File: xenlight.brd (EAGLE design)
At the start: 160.2 x 80.2 mm, 33 parts, among them IC1 MEGA16-A, IC14 FT232RL, IC2 74HC573D, IC3 74HC573D, IC4 74HC573D, IC5 74HC573D, IC6 74HC573D, IC7 74HC573D, X1 057-010-1, X2 057-010-1, X3 057-010-1, X4 057-010-1, X5 057-010-1, X6 057-010-1, X7 KUSBVX

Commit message: Second version of board, not for homemade production.
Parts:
- moved IC11 60.2 mm to (117.9, 68.4)
- moved X9 39.1 mm to (75.3, 8.61)
- moved IC4 38.6 mm to (100.8, 69.1), turned to 270 degrees
- moved R7 37.7 mm to (43.7, 15.5), turned to 0 degrees
- moved C5 34.8 mm to (46.8, 18.5), turned to 180 degrees
- moved C6 34.2 mm to (51.6, 7.37)
- moved R8 33.4 mm to (47.2, 13.9), turned to 270 degrees
- moved IC14 32.0 mm to (58.2, 15.4)
- moved L1 29.9 mm to (20.1, 12.0)
- moved R1 19.7 mm to (22.3, 28.1)
- moved C1 19.2 mm to (18.5, 4.47)
- moved IC12 19.1 mm to (119.1, 11.4)
- moved IC5 18.8 mm to (100.7, 11.9)
- moved X6 18.2 mm to (22.5, 19.6)
- moved IC13 17.7 mm to (119.3, 29.5)
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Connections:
- net GND: no longer IC12.6, IC12.7, IC12.8, IC13.6, IC13.7, IC13.8
- net VCC: now also IC12.6, IC12.7, IC12.8, IC13.6, IC13.7, IC13.8
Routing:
- net N$93: track 20.8 -> 139.3 mm
- net N$94: track 17.7 -> 129.1 mm
- net N$95: track 20.7 -> 124.6 mm
- net N$96: track 17.7 -> 114.2 mm
- net N$97: track 20.8 -> 110.0 mm
- net N$98: track 17.7 -> 97.3 mm
- net N$99: track 96.1 -> 21.3 mm, vias 2 -> 0
- net N$100: track 88.7 -> 24.4 mm, vias 2 -> 0
- net N$55: track 64.0 -> 7.12 mm, vias 2 -> 0
- net N$54: track 61.9 -> 7.12 mm, vias 2 -> 0
- net N$75: track 17.3 -> 70.4 mm
- net N$53: track 59.9 -> 7.12 mm, vias 2 -> 0
- net N$9: track 120.8 -> 69.9 mm, vias 2 -> 0
- net N$52: track 57.6 -> 7.12 mm, vias 2 -> 0
- net N$48: track 57.1 -> 7.12 mm, vias 2 -> 0
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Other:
- board size 160.2 x 80.2 mm -> 148.9 x 80.4 mm

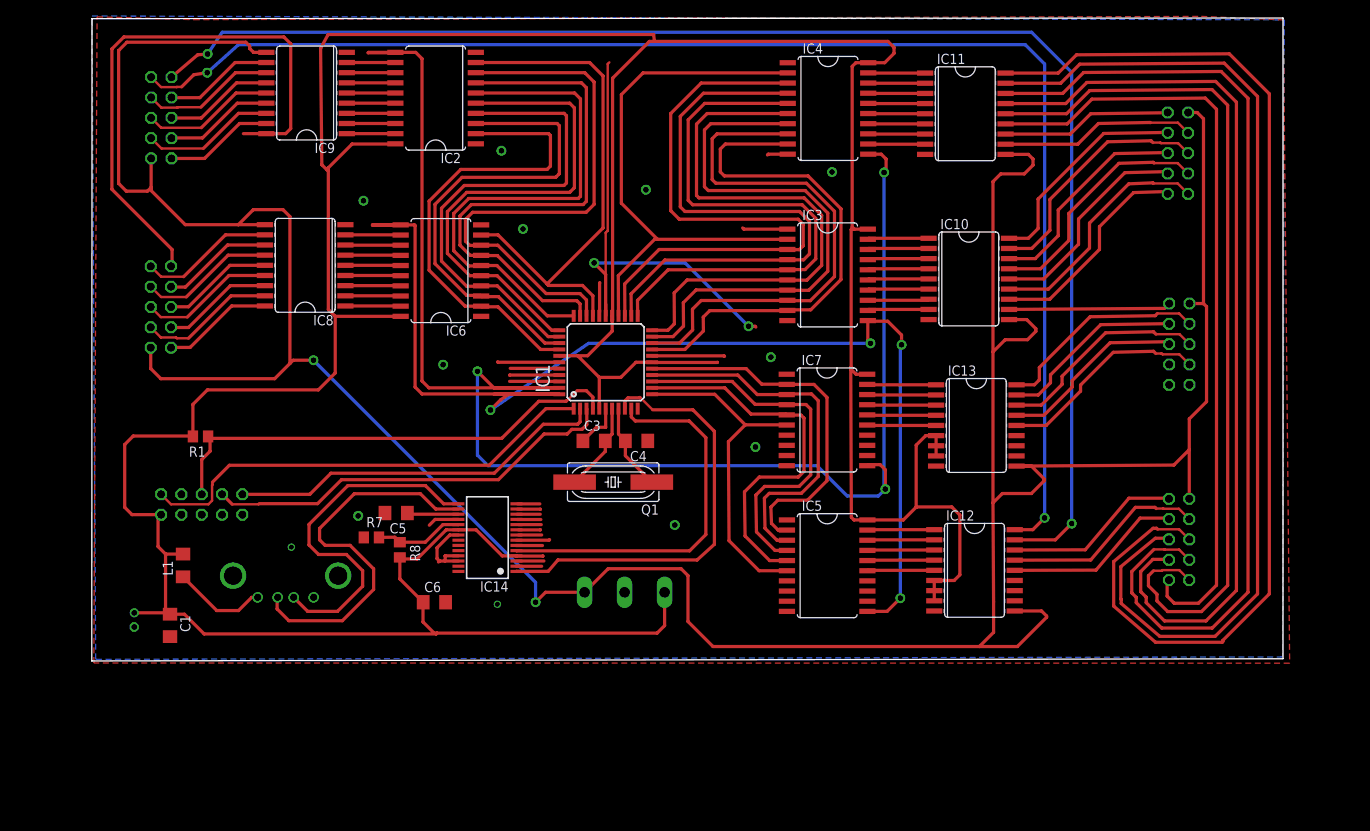
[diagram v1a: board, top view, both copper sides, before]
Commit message: Attempt to reduce size.
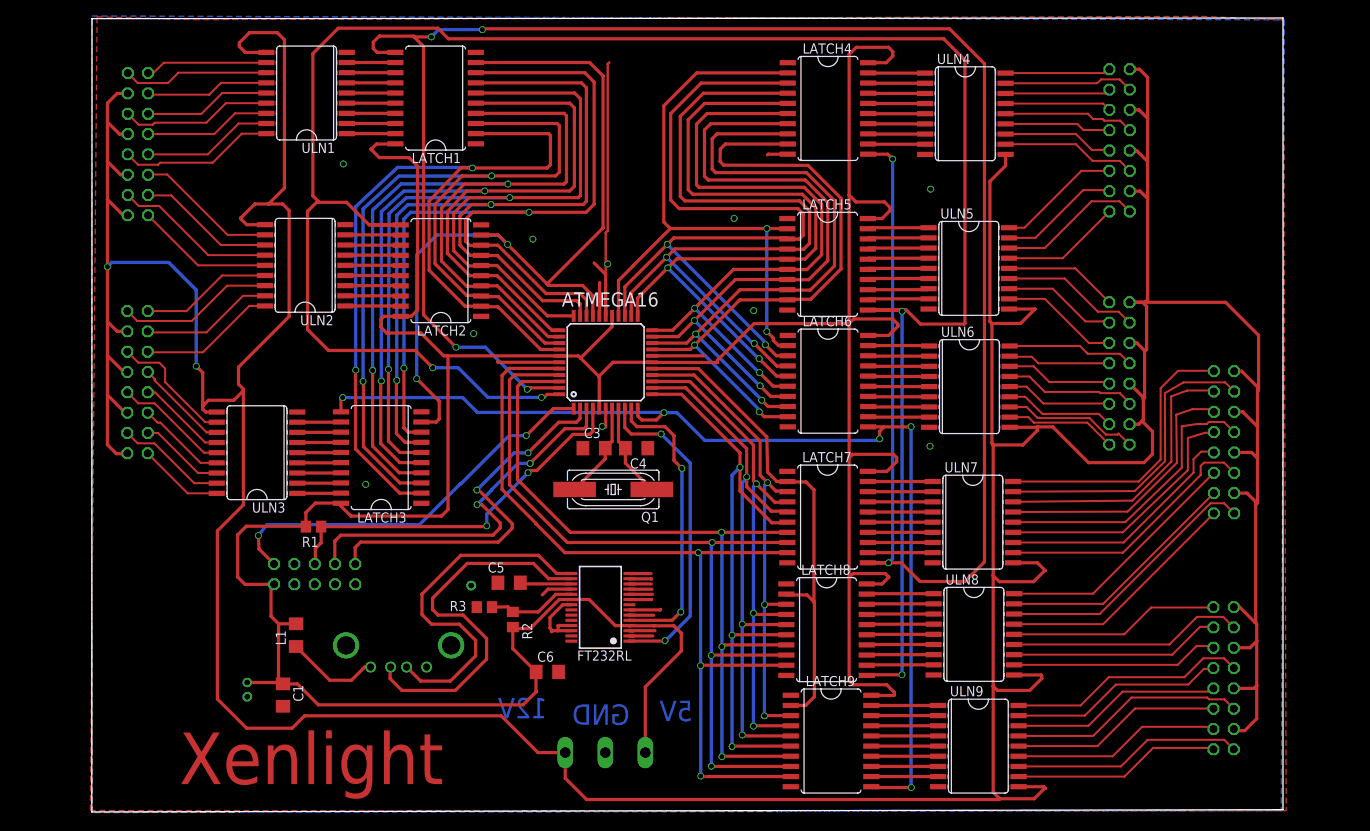
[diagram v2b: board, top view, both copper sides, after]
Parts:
- removed IC10, IC12, IC13: (no value), uln-udn2:SO18W
- removed IC14: FT232RL, ftdichip:SSOP28
- removed IC3, IC5, IC7: 74HC573D, 74xx-eu:SO20W
- removed R7: 10k, rcl:R0805
- removed R8: 4k7, rcl:R0805
- removed X9: (no value), con-ptr500:AK300/3
- added FT232RL: (no value), ftdichip:SSOP28
- added LATCH3, LATCH5, LATCH6, LATCH7, LATCH8, LATCH9: 74HC573D, 74xx-eu:SO20W
- added R2: 4k7, rcl:R0805
- added R3: 10k, rcl:R0805
- added SERWIS: (no value), con-panduit:057-010-1
- added ULN3: 3/1, uln-udn2:SO18W
- added ULN5: 2/2, uln-udn2:SO18W
- added ULN6: 3/2, uln-udn2:SO18W
- added ULN7: 1/3, uln-udn2:SO18W
- added ULN8: 2/3, uln-udn2:SO18W
- added ULN9: 3/3, uln-udn2:SO18W
- added ZASILANIE: (no value), con-ptr500:AK300/3
- ATMEGA16: value MEGA16-A -> (none)
- ULN1: value (none) -> 1/1
- ULN2: value (none) -> 2/1
- ULN4: value (none) -> 1/2
- X1, X2, X3, X4, X5, X6: value 057-010-1 -> (none); device con-panduit:057-010-1 -> con-panduit:057-016-1
- moved X6 129.6 mm to (150.2, -2.13), turned to 270 degrees
- moved X3 50.4 mm to (137.2, 65.1)
- moved X2 33.2 mm to (14.5, 34.9)
- moved X4 28.5 mm to (137.2, 36.0)
- moved X1 20.5 mm to (14.5, 64.6)
- moved R1 18.1 mm to (36.4, 16.8)
- moved C1 16.6 mm to (32.6, -4.24)
- moved C2 16.6 mm to (28.2, -3.56)
- moved C5 16.6 mm to (60.9, 9.80)
- moved L1 16.6 mm to (34.3, 3.25)
- moved C6 16.6 mm to (65.7, -1.35)
- moved X7 16.6 mm to (47.1, -0.74)
- moved X5 13.5 mm to (150.3, 27.4)
- moved C3 0.91 mm to (71.5, 26.6)
- moved C4 0.91 mm to (76.8, 26.6)
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- renumbered IC1 to ATMEGA16, IC11 to ULN4, IC2 to LATCH1, IC4 to LATCH4, IC6 to LATCH2, IC8 to ULN2, IC9 to ULN1
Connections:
- new net N$111: ULN2.11, X1.6
- new net N$112: ULN1.18, X1.7
- new net N$113: ULN1.17, X1.8
- new net N$115: ULN1.16, X1.10
- new net N$116: ULN1.15, X1.11
- new net N$124: LATCH8.14, ULN8.6
- new net N$128: LATCH8.13, ULN8.7
- new net N$129: LATCH8.12, ULN8.8
- new net N$130: LATCH7.14, ULN7.6
- new net N$131: LATCH7.13, ULN7.7
- new net N$132: LATCH7.12, ULN7.8
- new net N$133: ULN1.14, X1.12
- new net N$134: ULN1.13, X1.14
- new net N$135: ULN1.12, X1.15
- new net N$136: ULN1.11, X1.16
- new net N$137: ULN4.17, X3.3
- new net N$138: FT232RL.3
- new net N$139: FT232RL.11
- new net N$140: FT232RL.2
- new net N$141: FT232RL.9
- new net N$142: FT232RL.10
- new net N$143: FT232RL.6
- new net N$144: ATMEGA16.42, LATCH7.7, LATCH8.7, LATCH9.7
- new net N$145: ATMEGA16.41, LATCH7.8, LATCH8.8, LATCH9.8
- new net N$146: ATMEGA16.40, LATCH7.9, LATCH8.9, LATCH9.9
- new net N$147: FT232RL.23
- new net N$148: FT232RL.22
- new net N$149: FT232RL.13
- new net N$150: FT232RL.14
- new net N$151: FT232RL.12
- new net N$152: FT232RL.27
- new net N$153: FT232RL.28
- new net N$154: ULN4.16, X3.4
- new net N$155: ULN4.15, X3.6
- new net N$156: ULN4.14, X3.7
- new net N$157: ULN4.13, X3.8
- new net N$158: ULN4.12, X3.10
- new net N$159: ULN4.11, X3.11
- new net N$160: ULN5.18, X3.12
- new net N$161: ULN5.17, X3.14
- new net N$162: ULN5.16, X3.15
- new net N$163: ULN5.15, X3.16
- new net N$164: ULN5.14, X4.2
- new net N$165: ULN5.13, X4.3
- new net N$166: ULN5.12, X4.4
- new net N$167: ULN5.11, X4.6
- new net N$168: ULN6.18, X4.7
- new net N$169: ULN6.17, X4.8
- new net N$170: ULN6.16, X4.10
- new net N$171: ULN6.15, X4.11
- new net N$172: ULN6.14, X4.12
- new net N$173: ULN6.13, X4.14
- new net N$174: ULN6.12, X4.15
- new net N$175: ULN6.11, X4.16
- new net N$176: ULN7.18, X5.2
- new net N$177: ULN7.17, X5.3
- new net N$178: ULN7.16, X5.4
- new net N$179: ULN7.15, X5.6
- new net N$180: ULN7.14, X5.7
- new net N$181: ULN7.13, X5.8
- new net N$182: ULN7.12, X5.10
- new net N$183: ULN7.11, X5.11
- new net N$184: ULN8.18, X5.12
- new net N$185: ULN8.17, X5.14
- new net N$186: ULN8.16, X5.15
- new net N$187: ULN8.15, X5.16
- new net N$188: ULN8.14, X6.2
- new net N$189: ULN8.13, X6.3
- new net N$190: ULN8.12, X6.4
- new net N$191: ULN8.11, X6.6
- new net N$192: ULN9.18, X6.7
- new net N$193: ULN9.17, X6.8
- new net N$194: ULN9.16, X6.10
- new net N$195: ULN9.15, X6.11
- new net N$196: ULN9.14, X6.12
- new net N$197: ULN9.13, X6.14
- new net N$198: ULN9.12, X6.15
- new net N$199: ULN9.11, X6.16
- net 12V: now also ULN3.10, ULN5.10, ULN6.10, ULN7.10, ULN8.10, ULN9.10, X1.13, X1.5, X1.9, X2.13, X2.5, X2.9, X3.13, X3.5, X3.9, X4.13, X4.5, X4.9, X5.13, X5.5, X5.9, X6.1, X6.13, X6.5, X6.9, ZASILANIE.3; no longer IC10.10, IC12.10, IC13.10, X9.3
- net GND: now also FT232RL.18, FT232RL.21, FT232RL.25, FT232RL.26, FT232RL.7, LATCH3.1, LATCH3.10, LATCH5.1, LATCH5.10, LATCH6.1, LATCH6.10, LATCH7.1, LATCH7.10, LATCH8.1, LATCH8.10, LATCH9.1, LATCH9.10, R3.1, SERWIS.10, SERWIS.4, SERWIS.6, SERWIS.8, ULN3.9, ULN5.9, ULN6.9, ULN7.9, ULN8.9, ULN9.9, ZASILANIE.2; no longer IC10.9, IC12.9, IC13.9, IC14.18, IC14.21, IC14.25, IC14.26, IC14.7, IC3.1, IC3.10, IC5.1, IC5.10, IC5.7, IC5.8, IC5.9, IC7.1, IC7.10, IC7.7, IC7.8, IC7.9, R7.1, X5.10, X5.8, X5.9, X6.10, X6.4, X6.6, X6.8, X9.2
- net N$1: now also LATCH3.9
- net N$10: now also LATCH5.3, LATCH6.3; no longer IC3.3
- net N$100: now also ULN2.18, X2.12; no longer ULN4.11, X4.3
- net N$101: now also ULN2.17, X2.14; no longer IC13.15, X5.6
- net N$102: now also ULN2.16, X2.15; no longer IC12.18, X2.9
- net N$103: now also ULN2.15, X2.16; no longer IC12.17, X2.10
- net N$104: now also ULN2.14, X1.2; no longer IC13.14, X5.7
- net N$105: now also SERWIS.7; no longer X6.7
- net N$106: now also SERWIS.9; no longer X6.9
- net N$107: now also SERWIS.1; no longer X6.1
- net N$108: now also ULN2.13, X1.3; no longer IC13.18, X5.3
- net N$109: now also ULN2.12, X1.4; no longer IC13.17, X5.4
- net N$11: now also LATCH5.4, LATCH6.4; no longer IC3.4
- net N$110: now also LATCH5.12, ULN5.8; no longer IC10.8, IC3.12
- net N$119: now also FT232RL.15; no longer IC14.15
- net N$12: now also LATCH5.5, LATCH6.5; no longer IC3.5
- net N$120: now also FT232RL.1; no longer IC14.1
- net N$121: now also FT232RL.5; no longer IC14.5
- net N$122: now also FT232RL.16; no longer IC14.16
- net N$125: now also FT232RL.19, R2.1, R3.2; no longer IC14.19, R7.2, R8.1
- net N$126: now also FT232RL.17; no longer IC14.17
- net N$127: now also SERWIS.5; no longer X6.5
- net N$13: now also LATCH5.6, LATCH6.6; no longer IC3.6
- net N$14: now also LATCH5.7, LATCH6.7; no longer IC3.7
- net N$15: now also LATCH5.8, LATCH6.8; no longer IC3.8
- net N$16: now also LATCH5.9, LATCH6.9; no longer IC3.9
- net N$17: now also LATCH7.2, LATCH8.2, LATCH9.2; no longer IC5.2, IC7.2
- net N$18: now also LATCH7.3, LATCH8.3, LATCH9.3; no longer IC5.3, IC7.3
- net N$19: now also LATCH7.4, LATCH8.4, LATCH9.4; no longer IC5.4, IC7.4
- net N$2: now also LATCH3.8
- net N$20: now also LATCH7.5, LATCH8.5, LATCH9.5; no longer IC5.5, IC7.5
- net N$21: now also LATCH7.6, LATCH8.6, LATCH9.6; no longer IC5.6, IC7.6
- net N$22: now also LATCH5.11, LATCH8.11; no longer IC3.11, IC5.11
- net N$23: now also LATCH7.11; no longer IC7.11
- net N$3: now also LATCH3.7
- net N$4: now also LATCH3.6
- net N$40: now also LATCH5.19, ULN5.1; no longer IC10.1, IC3.19
- net N$41: now also LATCH5.18, ULN5.2; no longer IC10.2, IC3.18
- net N$42: now also LATCH5.17, ULN5.3; no longer IC10.3, IC3.17
- net N$43: now also LATCH5.16, ULN5.4; no longer IC10.4, IC3.16
- net N$44: now also LATCH5.15, ULN5.5; no longer IC10.5, IC3.15
- net N$45: now also LATCH5.14, ULN5.6; no longer IC10.6, IC3.14
- net N$46: now also LATCH5.13, ULN5.7; no longer IC10.7, IC3.13
- net N$47: now also LATCH3.19, ULN3.1; no longer IC12.16, X3.2
- net N$5: now also LATCH3.5
- net N$56: now also LATCH8.19, ULN8.1; no longer IC12.1, IC5.19
- net N$57: now also LATCH8.18, ULN8.2; no longer IC12.2, IC5.18
- net N$58: now also LATCH8.17, ULN8.3; no longer IC12.3, IC5.17
- net N$59: now also LATCH8.16, ULN8.4; no longer IC12.4, IC5.16
- net N$6: now also LATCH3.4
- net N$60: now also LATCH8.15, ULN8.5; no longer IC12.5, IC5.15
- net N$61: now also LATCH3.18, ULN3.2; no longer ULN2.18, X1.2
- net N$62: now also ULN4.18, X3.2; no longer ULN2.17, X1.3
- net N$63: now also LATCH3.17, ULN3.3; no longer ULN2.16, X1.4
- net N$64: now also LATCH7.19, ULN7.1; no longer IC13.1, IC7.19
- net N$65: now also LATCH7.18, ULN7.2; no longer IC13.2, IC7.18
- net N$66: now also LATCH7.17, ULN7.3; no longer IC13.3, IC7.17
- net N$67: now also LATCH7.16, ULN7.4; no longer IC13.4, IC7.16
- net N$68: now also LATCH7.15, ULN7.5; no longer IC13.5, IC7.15
- net N$69: now also LATCH3.16, ULN3.4; no longer ULN2.15, X1.5
- net N$7: now also LATCH3.3
- net N$70: now also LATCH3.15, ULN3.5; no longer ULN2.14, X1.6
- net N$71: now also LATCH3.14, ULN3.6; no longer ULN2.13, X1.7
- net N$72: now also LATCH3.13, ULN3.7; no longer ULN2.12, X1.8
- net N$73: now also LATCH3.12, ULN3.8; no longer ULN2.11, X1.9
- net N$74: now also ATMEGA16.11, LATCH3.11, LATCH6.11, LATCH9.11; no longer IC12.15, X3.3
- net N$75: now also LATCH6.19, ULN6.1; no longer ULN1.18, X1.10
- net N$76: now also LATCH6.18, ULN6.2; no longer ULN1.17, X2.2
- net N$77: now also LATCH6.17, ULN6.3; no longer ULN1.16, X2.3
- net N$78: now also LATCH6.16, ULN6.4; no longer ULN1.15, X2.4
- net N$79: now also LATCH6.15, ULN6.5; no longer ULN1.14, X2.5
- net N$8: now also LATCH3.2
- net N$80: now also LATCH6.14, ULN6.6; no longer ULN1.13, X2.6
- net N$81: now also LATCH6.13, ULN6.7; no longer ULN1.12, X2.7
- net N$82: now also LATCH6.12, ULN6.8; no longer ULN1.11, X2.8
- net N$83: now also ATMEGA16.29; no longer IC12.14, X3.4
- net N$84: now also LATCH9.19, ULN9.1; no longer IC10.18, X4.4
- net N$85: now also LATCH9.18, ULN9.2; no longer IC10.17, X4.5
- net N$86: now also LATCH9.17, ULN9.3; no longer IC10.16, X4.6
- net N$87: now also LATCH9.16, ULN9.4; no longer IC10.15, X4.7
- net N$88: now also LATCH9.15, ULN9.5; no longer IC10.14, X4.8
- net N$89: now also LATCH9.14, ULN9.6; no longer IC10.13, X4.9
- net N$9: now also LATCH5.2, LATCH6.2; no longer IC3.2
- net N$90: now also LATCH9.13, ULN9.7; no longer IC10.12, X4.10
- net N$91: now also LATCH9.12, ULN9.8; no longer IC10.11, X5.2
- net N$92: now also ULN3.18, X2.2; no longer IC13.16, X5.5
- net N$93: now also ULN3.17, X2.3; no longer ULN4.18, X3.5
- net N$94: now also ULN3.16, X2.4; no longer ULN4.17, X3.6
- net N$95: now also ULN3.15, X2.6; no longer ULN4.16, X3.7
- net N$96: now also ULN3.14, X2.7; no longer ULN4.15, X3.8
- net N$97: now also ULN3.13, X2.8; no longer ULN4.14, X3.9
- net N$98: now also ULN3.12, X2.10; no longer ULN4.13, X3.10
- net N$99: now also ULN3.11, X2.11; no longer ULN4.12, X4.2
- net VCC: now also FT232RL.20, FT232RL.4, LATCH3.20, LATCH5.20, LATCH6.20, LATCH7.20, LATCH8.20, LATCH9.20, R2.2, SERWIS.2, ZASILANIE.1; no longer IC12.6, IC12.7, IC12.8, IC13.6, IC13.7, IC13.8, IC14.20, IC14.4, IC3.20, IC5.20, IC7.20, R8.2, X6.2, X9.1
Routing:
- net 12V: track 398.5 -> 629.7 mm
- net N$103: track 181.4 -> 16.5 mm, vias 2 -> 0
- net N$102: track 176.3 -> 19.5 mm, vias 2 -> 0
- net N$93: track 139.3 -> 13.8 mm
- net N$22: track 154.5 -> 273.7 mm
- net N$94: track 129.1 -> 10.7 mm
- net N$95: track 124.6 -> 11.2 mm
- net N$146: track 0.00 -> 110.8 mm, vias 0 -> 3
- net N$74: track 25.5 -> 133.3 mm, vias 0 -> 5
- net N$145: track 0.00 -> 104.6 mm, vias 0 -> 3
- net N$96: track 114.2 -> 14.3 mm
- net N$97: track 110.0 -> 11.2 mm
- net N$144: track 0.00 -> 98.4 mm, vias 0 -> 3
- net N$98: track 97.3 -> 11.9 mm
- net N$23: track 192.2 -> 274.3 mm, vias 3 -> 6
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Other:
- board size 148.9 x 80.4 mm -> 148.9 x 99.2 mm
- board text added: "12V"
- board text added: "5V"
- board text added: "GND"
- board text added: "Xenlight"

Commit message: Another attempts to reduce size and reroute.
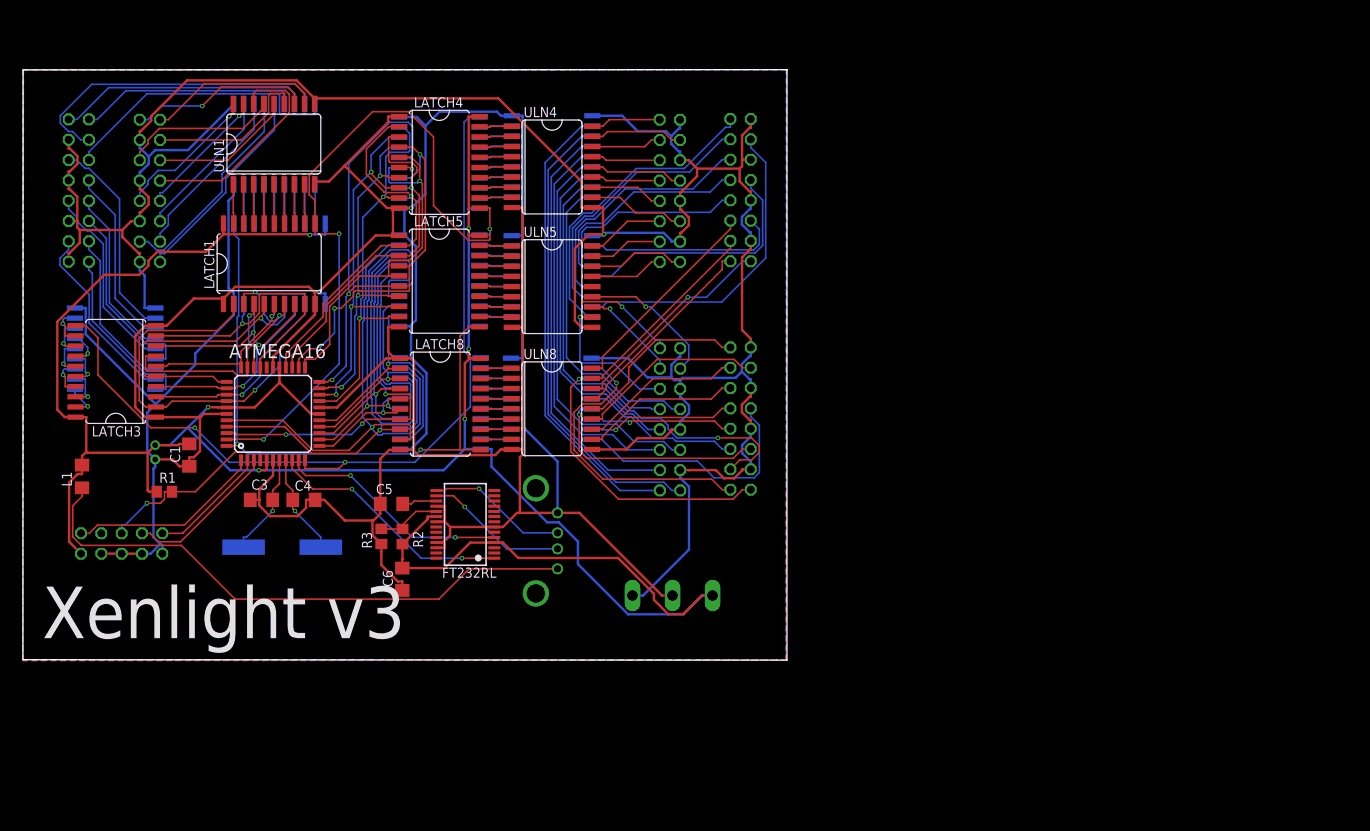
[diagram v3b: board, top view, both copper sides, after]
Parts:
- moved ULN9 68.8 mm to (66.2, 32.8), flipped to the bottom, turned to 90 degrees
- moved X6 68.5 mm to (89.8, 30.3)
- moved X5 68.2 mm to (89.8, 58.9)
- moved LATCH9 64.5 mm to (52.3, 32.2), flipped to the bottom, turned to 90 degrees
- moved ULN7 60.9 mm to (66.2, 48.1), flipped to the bottom, turned to 90 degrees
- moved ULN8 59.8 mm to (66.2, 31.5)
- moved ULN6 59.6 mm to (66.3, 63.1), flipped to the bottom, turned to 90 degrees
- moved LATCH7 56.8 mm to (52.2, 47.6), flipped to the bottom, turned to 90 degrees
- moved X3 56.6 mm to (81.0, 58.8)
- moved X4 56.5 mm to (81.0, 30.2)
- moved LATCH8 55.9 mm to (52.3, 32.1)
- moved LATCH6 55.7 mm to (52.2, 62.3), flipped to the bottom, turned to 90 degrees
- moved ULN5 52.1 mm to (66.3, 46.8)
- moved ULN4 52.1 mm to (66.3, 61.8)
- moved LATCH4 49.1 mm to (52.2, 62.4)
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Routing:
- net GND: track 76.0 -> 489.8 mm, vias 11 -> 2
- net 12V: track 629.7 -> 327.7 mm, vias 2 -> 1
- net N$22: track 273.7 -> 77.6 mm, vias 4 -> 2
- net N$23: track 274.3 -> 89.8 mm, vias 6 -> 3
- net VCC: track 411.0 -> 311.2 mm, vias 0 -> 6
- net N$4: track 114.3 -> 22.2 mm, vias 2 -> 1
- net N$6: track 117.2 -> 30.9 mm
- net N$2: track 114.8 -> 28.7 mm
- net N$7: track 117.2 -> 35.9 mm
- net N$3: track 111.2 -> 31.1 mm, vias 2 -> 1
- net N$5: track 111.8 -> 37.9 mm, vias 2 -> 1
- net N$1: track 102.1 -> 36.2 mm, vias 2 -> 1
- net N$8: track 116.5 -> 51.6 mm, vias 2 -> 1
- net N$123: track 11.8 -> 72.0 mm
- net N$10: track 96.7 -> 44.4 mm, vias 2 -> 1
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- added copper zone on layer 1, net N$200
- removed copper zone on layer 1, net GND
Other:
- board size 148.9 x 99.2 mm -> 95.5 x 73.8 mm
- board text added: "Dawid Karczewski 2014"
- board text added: "Xenlight v3"
- board text removed: "GND"
- board text removed: "Xenlight"
